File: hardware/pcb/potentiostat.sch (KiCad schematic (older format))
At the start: 58 parts

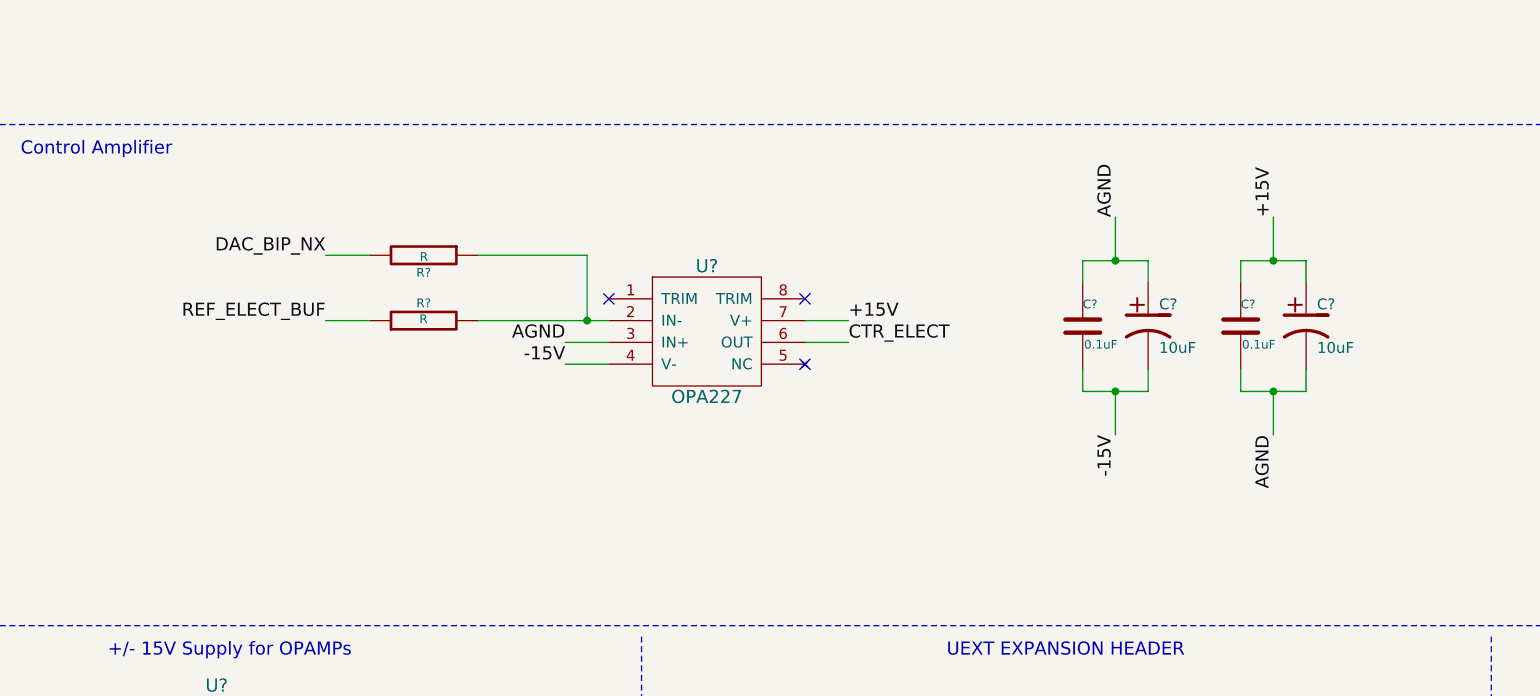
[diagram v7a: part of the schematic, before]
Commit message: Modified control amp schematic a bit to make it cleaner.
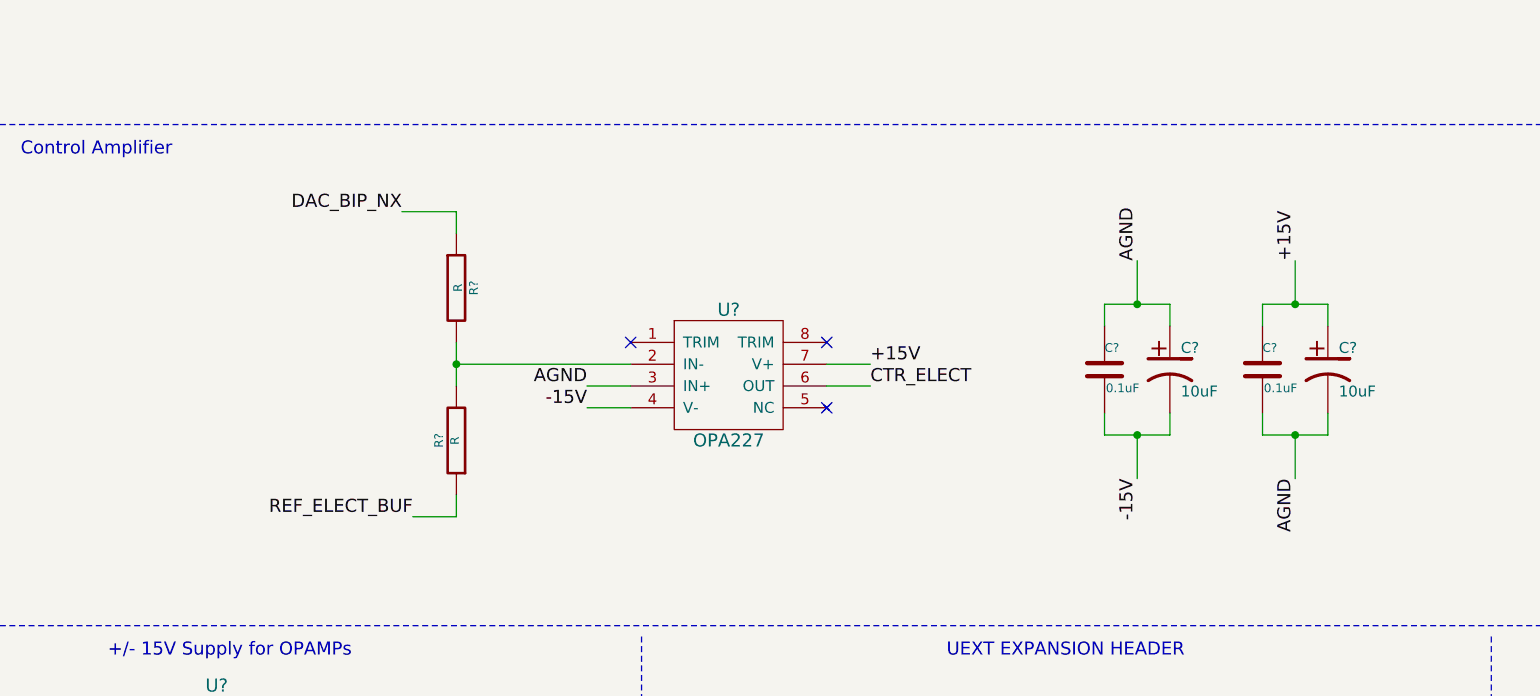
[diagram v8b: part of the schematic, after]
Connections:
- net DAC_BIP_NX: now also R?.1; no longer R?.2
- net at R?.2, U?.2 (IN-): now also R?.2; no longer R?.1
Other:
- moved on the sheet: C?, R?, U?
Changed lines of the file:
@@
 Sheet 1 1
 Title ""
-Date "16 may 2016"
+Date "17 may 2016"
 Rev ""
 Comp ""
@@
 L OPA227 U?
 U 1 1 5736DD28
-P 9650 10150
-F 0 "U?" H 9650 10450 60  0000 C CNN
-F 1 "OPA227" H 9650 9850 60  0000 C CNN
-F 2 "~" H 9750 10150 60  0000 C CNN
-F 3 "~" H 9750 10150 60  0000 C CNN
-	1    9650 10150
+P 9750 10350
+F 0 "U?" H 9750 10650 60  0000 C CNN
+F 1 "OPA227" H 9750 10050 60  0000 C CNN
+F 2 "~" H 9850 10350 60  0000 C CNN
+F 3 "~" H 9850 10350 60  0000 C CNN
+	1    9750 10350
 	1    0    0    -1
 $EndComp
 Text Notes 6500 9350 0    60   ~ 0
 Control Amplifier
-NoConn ~ 9200 10000
-NoConn ~ 10100 10000
-Text Label 9000 10200 2    60   ~ 0
+NoConn ~ 9300 10200
+NoConn ~ 10200 10200
+Text Label 9100 10400 2    60   ~ 0
 AGND
 $Comp
 L R R?
 U 1 1 5737532F
-P 8350 9800
-F 0 "R?" V 8430 9800 40  0000 C CNN
-F 1 "R" V 8357 9801 40  0000 C CNN
-F 2 "~" V 8280 9800 30  0000 C CNN
-F 3 "~" H 8350 9800 30  0000 C CNN
-	1    8350 9800
-	0    1    1    0
+P 8500 9950
+F 0 "R?" V 8580 9950 40  0000 C CNN
+F 1 "R" V 8507 9951 40  0000 C CNN
+F 2 "~" V 8430 9950 30  0000 C CNN
+F 3 "~" H 8500 9950 30  0000 C CNN
+	1    8500 9950
+	1    0    0    -1
 $EndComp
 $Comp
 L R R?
 U 1 1 5737533E
-P 8350 10100
-F 0 "R?" V 8430 10100 40  0000 C CNN
-F 1 "R" V 8357 10101 40  0000 C CNN
-F 2 "~" V 8280 10100 30  0000 C CNN
-F 3 "~" H 8350 10100 30  0000 C CNN
-	1    8350 10100
-	0    -1   -1   0
-$EndComp
-Text Label 7900 9800 2    60   ~ 0
+P 8500 10650
+F 0 "R?" V 8580 10650 40  0000 C CNN
+F 1 "R" V 8507 10651 40  0000 C CNN
+F 2 "~" V 8430 10650 30  0000 C CNN
+F 3 "~" H 8500 10650 30  0000 C CNN
+	1    8500 10650
+	-1   0    0    1
+$EndComp
+Text Label 8250 9600 2    60   ~ 0
 DAC_BIP_NX
 Wire Wire Line
@@
 Text Label 9100 7900 0    60   ~ 0
 REF_ELECT_BUF
-Wire Wire Line
-	8100 9800 7900 9800
-Wire Wire Line
-	8100 10100 7900 10100
-Text Label 7900 10100 2    60   ~ 0
+Text Label 8300 11000 2    60   ~ 0
 REF_ELECT_BUF
 Wire Wire Line
-	9200 10200 9000 10200
-Wire Wire Line
-	9200 10300 9000 10300
-Text Label 9000 10300 2    60   ~ 0
+	9300 10400 9100 10400
+Wire Wire Line
+	9300 10500 9100 10500
+Text Label 9100 10500 2    60   ~ 0
 -15V
 Wire Wire Line
-	10100 10100 10300 10100
-Text Label 10300 10100 0    60   ~ 0
+	10200 10300 10400 10300
+Text Label 10400 10300 0    60   ~ 0
 +15V
 Wire Wire Line
-	10100 10200 10300 10200
-Text Label 10300 10200 0    60   ~ 0
+	10200 10400 10400 10400
+Text Label 10400 10400 0    60   ~ 0
 CTR_ELECT
-NoConn ~ 10100 10300
-Wire Wire Line
-	8600 10100 9200 10100
-Wire Wire Line
-	8600 9800 9100 9800
-Wire Wire Line
-	9100 9800 9100 10100
-Connection ~ 9100 10100
+NoConn ~ 10200 10500
+Wire Wire Line
+	8500 10300 9300 10300
 $Comp
 L C C?
 U 1 1 57376739
-P 12100 10125
-F 0 "C?" H 12100 10225 40  0000 L CNN
-F 1 "0.1uF" H 12106 10040 40  0000 L CNN
-F 2 "~" H 12138 9975 30  0000 C CNN
-F 3 "~" H 12100 10125 60  0000 C CNN
-	1    12100 10125
+P 12200 10325
+F 0 "C?" H 12200 10425 40  0000 L CNN
+F 1 "0.1uF" H 12206 10240 40  0000 L CNN
+F 2 "~" H 12238 10175 30  0000 C CNN
+F 3 "~" H 12200 10325 60  0000 C CNN
+	1    12200 10325
 	1    0    0    -1
 $EndComp
@@
 L C C?
 U 1 1 5737673F
-P 11375 10125
-F 0 "C?" H 11375 10225 40  0000 L CNN
-F 1 "0.1uF" H 11381 10040 40  0000 L CNN
-F 2 "~" H 11413 9975 30  0000 C CNN
-F 3 "~" H 11375 10125 60  0000 C CNN
-	1    11375 10125
+P 11475 10325
+F 0 "C?" H 11475 10425 40  0000 L CNN
+F 1 "0.1uF" H 11481 10240 40  0000 L CNN
+F 2 "~" H 11513 10175 30  0000 C CNN
+F 3 "~" H 11475 10325 60  0000 C CNN
+	1    11475 10325
 	1    0    0    -1
 $EndComp
@@
 L CP1 C?
 U 1 1 57376745
-P 12400 10125
-F 0 "C?" H 12450 10225 50  0000 L CNN
-F 1 "10uF" H 12450 10025 50  0000 L CNN
-F 2 "~" H 12400 10125 60  0000 C CNN
-F 3 "~" H 12400 10125 60  0000 C CNN
-	1    12400 10125
+P 12500 10325
+F 0 "C?" H 12550 10425 50  0000 L CNN
+F 1 "10uF" H 12550 10225 50  0000 L CNN
+F 2 "~" H 12500 10325 60  0000 C CNN
+F 3 "~" H 12500 10325 60  0000 C CNN
+	1    12500 10325
 	1    0    0    -1
 $EndComp
@@
 L CP1 C?
 U 1 1 5737674B
-P 11675 10125
-F 0 "C?" H 11725 10225 50  0000 L CNN
-F 1 "10uF" H 11725 10025 50  0000 L CNN
-F 2 "~" H 11675 10125 60  0000 C CNN
-F 3 "~" H 11675 10125 60  0000 C CNN
-	1    11675 10125
-	1    0    0    -1
-$EndComp
-Text Label 11525 9625 1    60   ~ 0
-AGND
-Text Label 11525 10625 3    60   ~ 0
+P 11775 10325
+F 0 "C?" H 11825 10425 50  0000 L CNN
+F 1 "10uF" H 11825 10225 50  0000 L CNN
+F 2 "~" H 11775 10325 60  0000 C CNN
+F 3 "~" H 11775 10325 60  0000 C CNN
+	1    11775 10325
+	1    0    0    -1
+$EndComp
+Text Label 11625 9825 1    60   ~ 0
+AGND
+Text Label 11625 10825 3    60   ~ 0
 -15V
-Text Label 12250 10625 3    60   ~ 0
-AGND
-Text Label 12250 9625 1    60   ~ 0
+Text Label 12350 10825 3    60   ~ 0
+AGND
+Text Label 12350 9825 1    60   ~ 0
 +15V
 Wire Wire Line
-	11675 10425 11675 10325
-Wire Wire Line
-	11375 10425 11675 10425
-Wire Wire Line
-	11375 10425 11375 10325
-Wire Wire Line
-	11525 10425 11525 10625
-Connection ~ 11525 10425
-Wire Wire Line
-	11675 9825 11675 9925
-Wire Wire Line
-	11375 9825 11675 9825
-Wire Wire Line
-	11375 9825 11375 9925
-Wire Wire Line
-	11525 9825 11525 9625
-Connection ~ 11525 9825
-Wire Wire Line
-	12100 9925 12100 9825
-Wire Wire Line
-	12100 9825 12400 9825
-Wire Wire Line
-	12400 9825 12400 9925
-Wire Wire Line
-	12250 9825 12250 9625
-Connection ~ 12250 9825
-Wire Wire Line
-	12100 10325 12100 10425
-Wire Wire Line
-	12100 10425 12400 10425
-Wire Wire Line
-	12400 10425 12400 10325
-Wire Wire Line
-	12250 10425 12250 10625
-Connection ~ 12250 10425
+	11775 10625 11775 10525
+Wire Wire Line
+	11475 10625 11775 10625
+Wire Wire Line
+	11475 10625 11475 10525
+Wire Wire Line
+	11625 10625 11625 10825
+Connection ~ 11625 10625
+Wire Wire Line
+	11775 10025 11775 10125
+Wire Wire Line
+	11475 10025 11775 10025
+Wire Wire Line
+	11475 10025 11475 10125
+Wire Wire Line
+	11625 10025 11625 9825
+Connection ~ 11625 10025
+Wire Wire Line
+	12200 10125 12200 10025
+Wire Wire Line
+	12200 10025 12500 10025
+Wire Wire Line
+	12500 10025 12500 10125
+Wire Wire Line
+	12350 10025 12350 9825
+Connection ~ 12350 10025
+Wire Wire Line
+	12200 10525 12200 10625
+Wire Wire Line
+	12200 10625 12500 10625
+Wire Wire Line
+	12500 10625 12500 10525
+Wire Wire Line
+	12350 10625 12350 10825
+Connection ~ 12350 10625
 Wire Wire Line
 	7150 4200 7550 4200
@@
 Text Notes 350  -2300 0    200  ~ 0
 1. Add analog input for reference electrode (buffered).  Could just take -[10V, 10V] analog input from noah motion controller.
+Wire Wire Line
+	8500 10200 8500 10400
+Connection ~ 8500 10300
+Wire Wire Line
+	8500 9700 8500 9600
+Wire Wire Line
+	8500 10900 8500 11000
+Wire Wire Line
+	8500 9600 8250 9600
+Wire Wire Line
+	8500 11000 8300 11000
 $EndSCHEMATC
